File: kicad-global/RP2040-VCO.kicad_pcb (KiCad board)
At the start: 2 copper layers, 207 x 128.5 mm, 46 parts, among them J1 V/oct, J2 Power Input, J3 Inv CV, J4 Out, U1 TL074, U2 Seed_XIAO_RP2040

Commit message: finished schem and started pcb
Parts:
- added C11: 100pF, Capacitor_SMD:C_0805_2012Metric_Pad1.18x1.45mm_HandSolder, F.Cu at (55.0, 170.0)
- added CHORD1: 10k, Kicad-perso:Pot-bourns-alpha, F.Cu at (42.5, 70.5)
- added INV1: 10k, Kicad-perso:Pot-bourns-alpha, F.Cu at (42.5, 88.3)
- added SW1: SW_SPDT, Kicad-perso:SW_Toggle_Blue_wSlots, F.Cu at (40.6, 109.2)
- added SW2: SW_MEC_LOW_PROF_LED, Kicad-perso:PB01-109TL, F.Cu at (45.7, 121.9)
- added U3: AP2210K-5.0TRG1, Kicad-perso:SOT95P282X130-5N, F.Cu at (50.0, 170.0)
- C3, C4: footprint Capacitor_THT:CP_Radial_D5.0mm_P2.00mm -> Capacitor_SMD:CP_Elec_4x5.4
- C8: renamed from C11; value 10uF -> 1uF
- J1, J3, J4: footprint Synth:Thonkiconn -> Kicad-perso:Thonkiconn
- TUNE1: footprint Synth:Pot-bourns-alpha -> Kicad-perso:Pot-bourns-alpha
- moved J4 108.3 mm to (35.6, 116.8)
- moved J1 106.3 mm to (35.6, 131.4)
- moved TUNE1 99.3 mm to (43.1, 51.8)
- moved J3 90.0 mm to (45.7, 131.4)
- moved R8 39.1 mm to (80.0, 115.0), turned to -90 degrees
- moved C3 38.9 mm to (71.1, 91.4)
- moved J2 17.0 mm to (34.3, 98.3), turned to -90 degrees
- moved U1 13.6 mm to (70.0, 175.0)
- moved C4 9.37 mm to (71.7, 100.3)
- renumbered C8 to C12, C12 to C13, C13 to C14, C14 to C15, C15 to C16, R15 to R12, R12 to R13, R13 to R14, R14 to R15
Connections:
- C12 pad 1: +12V -> +5V
- C8 pad 1: +5V -> +12V
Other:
- outline, holes or cut-outs redrawn
- board text added: "4HP"
- board text removed: "12HP"
- board text removed: "board 2/2"

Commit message: update schem + begin routing
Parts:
- removed H2, H3: MountingHole_Pad, Synth:Doepfer Mounting hole
- added J4: Conn_01x06_Female, Connector_PinSocket_2.54mm:PinSocket_1x06_P2.54mm_Vertical, B.Cu at (75.8, 49.5)
- added J5: Conn_01x08_Female, Connector_PinSocket_2.54mm:PinSocket_1x08_P2.54mm_Vertical, B.Cu at (75.8, 95.6)
- added J6: Conn_01x06_Male, Connector_PinHeader_2.54mm:PinHeader_1x06_P2.54mm_Horizontal, B.Cu at (36.1, 49.5)
- added J7: Conn_01x08_Male, Connector_PinHeader_2.54mm:PinHeader_1x08_P2.54mm_Horizontal, B.Cu at (36.1, 95.6)
- C3, C4, J2, U2: moved to F.Cu
- moved R13 133.4 mm to (58.5, 51.8)
- moved R1 133.0 mm to (40.0, 54.6)
- moved C7 129.7 mm to (58.5, 55.9), turned to 180 degrees
- moved R5 127.6 mm to (40.0, 52.1)
- moved R16 126.8 mm to (47.1, 51.9)
- moved D4 121.0 mm to (58.1, 64.4)
- moved R2 120.7 mm to (40.0, 57.1)
- moved U1 120.3 mm to (52.8, 55.9)
- moved R6 120.3 mm to (51.0, 61.6)
- moved R11 119.3 mm to (58.5, 53.8)
- moved D3 118.7 mm to (58.1, 66.8)
- moved R8 118.3 mm to (58.5, 60.0)
- moved R15 118.1 mm to (47.1, 53.9)
- moved R14 116.0 mm to (58.5, 62.0), turned to 180 degrees
- moved R7 112.7 mm to (58.5, 58.0)
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- renumbered C9 to C8, C8 to C9, J4 to J8, R8 to R10, R10 to R12, R15 to R14, R14 to R15, R9 to R8, R12 to R9
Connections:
- net Net-(C16-Pad1) renamed /OutJack
- net Net-(CHORD1-Pad2) renamed /ChordPot
- net Net-(INV1-Pad2) renamed /InvPot
- net Net-(J1-PadT) renamed /V/octJack
- net Net-(J3-PadT) renamed /InvJack
- net Net-(R1-Pad1) renamed /TunePot
- C15 pad 2: Net-(C15-Pad2) -> GND
- D4 pad 2: Net-(C15-Pad2) -> GND
- R14 pad 1: Net-(C15-Pad2) -> GND
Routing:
- net +12V: track 0.00 -> 24.2 mm
- net -12V: track 0.00 -> 9.18 mm
- net Net-(R11-Pad2): track 0.00 -> 5.17 mm
- net /InvPot: track 0.00 -> 2.92 mm
- net /TunePot: track 0.00 -> 2.91 mm
- net /ChordPot: track 0.00 -> 2.91 mm
- net Net-(R11-Pad1): track 0.00 -> 2.41 mm
- net GND: vias 17 -> 9
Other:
- board size 207 x 128.5 mm -> 96.9 x 128.5 mm
- board text added: "RP2040 VCO V1.0 BleepSound 2023"
- board text added: "board 2/2"
- board text removed: "Double MS-20 VCF V1.2 BleepSound 2022"

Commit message: Routing finished
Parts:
- moved C16 38.0 mm to (39.6, 67.8)
- moved D2 28.5 mm to (44.0, 68.1)
- moved D1 28.5 mm to (44.0, 65.7)
- moved J7 27.8 mm to (36.3, 67.8)
- moved J5 27.8 mm to (75.8, 67.8)
- moved R3 26.6 mm to (39.6, 74.1)
- moved R4 26.6 mm to (39.6, 72.1)
- moved C3 21.7 mm to (40.9, 93.5), turned to 90 degrees
- moved C12 16.8 mm to (46.1, 91.1), turned to -90 degrees
- moved U3 13.6 mm to (49.0, 91.3), turned to 90 degrees
- moved C11 11.6 mm to (51.9, 91.1), turned to -90 degrees
- moved C9 10.8 mm to (48.9, 94.5), turned to 0 degrees
- moved C4 7.31 mm to (57.0, 93.5), turned to -90 degrees
- moved J2 3.81 mm to (54.0, 100.7), turned to -90 degrees
- moved J6 0.25 mm to (36.3, 49.5)
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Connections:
- J5 pad 1: +12V -> /OutJack
- J5 pad 2: GND -> /InvJack
- J5 pad 4: /InvJack -> GND
- J5 pad 5: /OutJack -> /SW_0
- J5 pad 7: /SW_0 -> /SW_1
- J5 pad 8: /SW_1 -> +12V
- J7 pad 1: +12V -> /OutJack
- J7 pad 2: GND -> /InvJack
- J7 pad 4: /InvJack -> GND
- J7 pad 5: /OutJack -> /SW_0
- J7 pad 7: /SW_0 -> /SW_1
- J7 pad 8: /SW_1 -> +12V
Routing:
- net +12V: track 24.2 -> 158.2 mm, vias 0 -> 2
- net /InvJack: track 0.00 -> 117.2 mm, vias 0 -> 2
- net +5V: track 0.00 -> 97.0 mm, vias 0 -> 1
- net +3V3: track 0.00 -> 84.7 mm, vias 0 -> 2
- net /V/octJack: track 0.00 -> 77.3 mm
- net /Push_SW: track 0.00 -> 77.0 mm
- net /OutJack: track 0.00 -> 71.3 mm
- net -12V: track 9.18 -> 66.8 mm, vias 0 -> 1
- net /SW_0: track 0.00 -> 55.4 mm
- net /InvPot: track 2.92 -> 48.1 mm
- net /V/oct: track 0.00 -> 44.7 mm
- net /SW_1: track 0.00 -> 41.3 mm
- net Net-(C14-Pad1): track 0.00 -> 38.9 mm, vias 0 -> 2
- net /Inv: track 0.00 -> 33.3 mm
- net /Tune: track 0.00 -> 31.9 mm
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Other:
- board size 96.9 x 128.5 mm -> 96.8 x 128.5 mm

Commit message: update VCO pcb
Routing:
- net GND: vias 69 -> 70

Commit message: update to v1.1
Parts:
- removed the J6 at (36.3, 49.5)
- removed the J7 at (36.3, 67.8)
- added H2: SpacerHoles, MountingHole:MountingHole_3.2mm_M3, F.Cu at (68.0, 96.0)
- added H3: SpacerHoles, MountingHole:MountingHole_3.2mm_M3, F.Cu at (90.5, 96.0)
- added J1: Conn_01x06_Male, Connector_PinHeader_2.54mm:PinHeader_1x06_P2.54mm_Vertical, F.Cu at (69.7, 49.5)
- added J2: Conn_01x08_Male, Connector_PinHeader_2.54mm:PinHeader_1x08_P2.54mm_Vertical, F.Cu at (53.3, 67.8)
- D1: renamed from D3; footprint Diode_SMD:D_SOD-123 -> Kicad-perso:D_SOD-123
- D2: renamed from D4; footprint Diode_SMD:D_SOD-123 -> Kicad-perso:D_SOD-123
- D3: renamed from D1; footprint Diode_SMD:D_SOD-123 -> Kicad-perso:D_SOD-123
- D4: renamed from D2; footprint Diode_SMD:D_SOD-123 -> Kicad-perso:D_SOD-123
- J8: renamed from J2; moved to B.Cu
- U1: footprint Package_SO:SOIC-14_3.9x8.7mm_P1.27mm -> Kicad-perso:SOIC-14_3.9x8.7mm_P1.27mm
- U3: renamed from U2; moved to B.Cu
- moved C10 43.4 mm to (56.9, 118.1), turned to 0 degrees
- moved C9 40.8 mm to (56.9, 115.6), turned to 0 degrees
- moved J8 40.6 mm to (60.3, 140.9), turned to 0 degrees
- moved C7 38.2 mm to (56.9, 113.0), turned to 0 degrees
- moved C14 36.2 mm to (54.0, 127.3)
- moved C13 36.0 mm to (64.4, 124.8)
- moved C12 36.0 mm to (58.6, 124.8)
- moved C16 36.0 mm to (61.4, 128.2)
- moved U2 36.0 mm to (61.5, 125.0)
- moved C6 36.0 mm to (57.0, 110.5), turned to 0 degrees
- moved C15 35.7 mm to (69.0, 127.2)
- moved C11 35.4 mm to (66.1, 118.1), turned to 180 degrees
- moved U3 32.7 mm to (61.5, 110.5), turned to 0 degrees
- moved C8 31.7 mm to (66.1, 113.0), turned to 180 degrees
- moved C5 29.3 mm to (66.1, 107.5), turned to 0 degrees
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- renumbered C16 to C1, C5 to C10, C8 to C11, C11 to C13, C3 to C14, C4 to C15, C9 to C16, C7 to C2, C6 to C3, C14 to C4, C13 to C5, C2 to C6, C15 to C7, C10 to C8, C1 to C9, J8 to J3, J1 to J4, J3 to J5, J4 to J6, J5 to J7, R5 to R1, R4 to R10, R6 to R11, R14 to R12, R3 to R13, R12 to R14, R10 to R15, R9 to R16, R1 to R2, R2 to R3, R13 to R4, R16 to R5, R11 to R6, R15 to R7, R7 to R8, R8 to R9, U3 to U2
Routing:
- net +3V3: track 84.7 -> 128.6 mm, vias 2 -> 0
- net /Chord: track 21.6 -> 61.2 mm, vias 0 -> 1
- net /Tune: track 31.9 -> 68.4 mm, vias 0 -> 1
- net /SW_1: track 41.3 -> 76.7 mm, vias 0 -> 2
- net /Inv: track 33.3 -> 66.9 mm, vias 0 -> 3
- net +12V: track 158.2 -> 133.8 mm, vias 2 -> 3
- net Net-(C1-Pad2): track 23.2 -> 2.90 mm
- net -12V: track 66.8 -> 84.6 mm, vias 1 -> 2
- net +5V: track 97.0 -> 111.7 mm, vias 1 -> 0
- net /SW_0: track 55.4 -> 67.8 mm
- net /Push_SW: track 77.0 -> 87.9 mm
- net GND: track 3.90 -> 14.7 mm, vias 70 -> 55
- net Net-(U1B-+): track 11.9 -> 22.2 mm
- net /InvJack: track 117.2 -> 107.3 mm, vias 2 -> 0
- net /V/oct: track 44.7 -> 49.8 mm
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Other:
- board size 96.8 x 128.5 mm -> 80 x 128.5 mm
- board text added: "RP2040 VCO V1.1 BleepSound 2023"

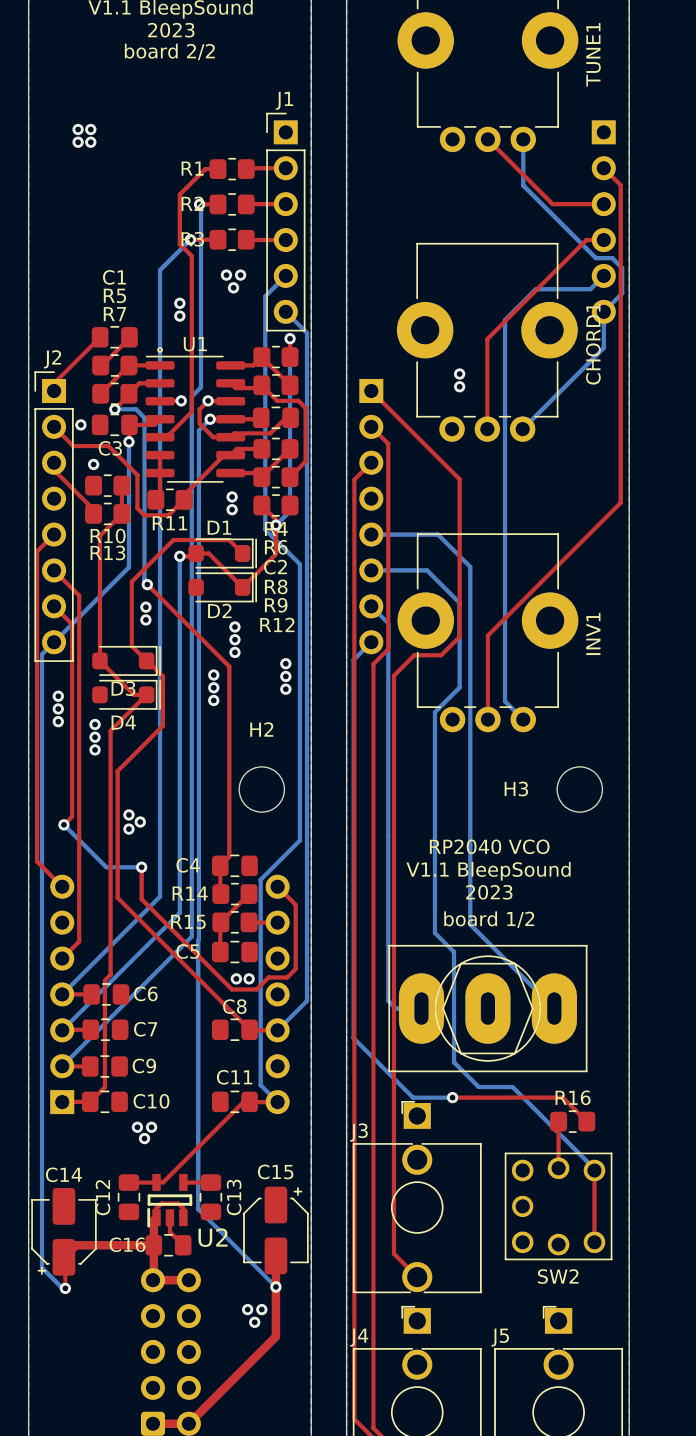
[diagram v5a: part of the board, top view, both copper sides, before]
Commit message: update board with pullup on switch
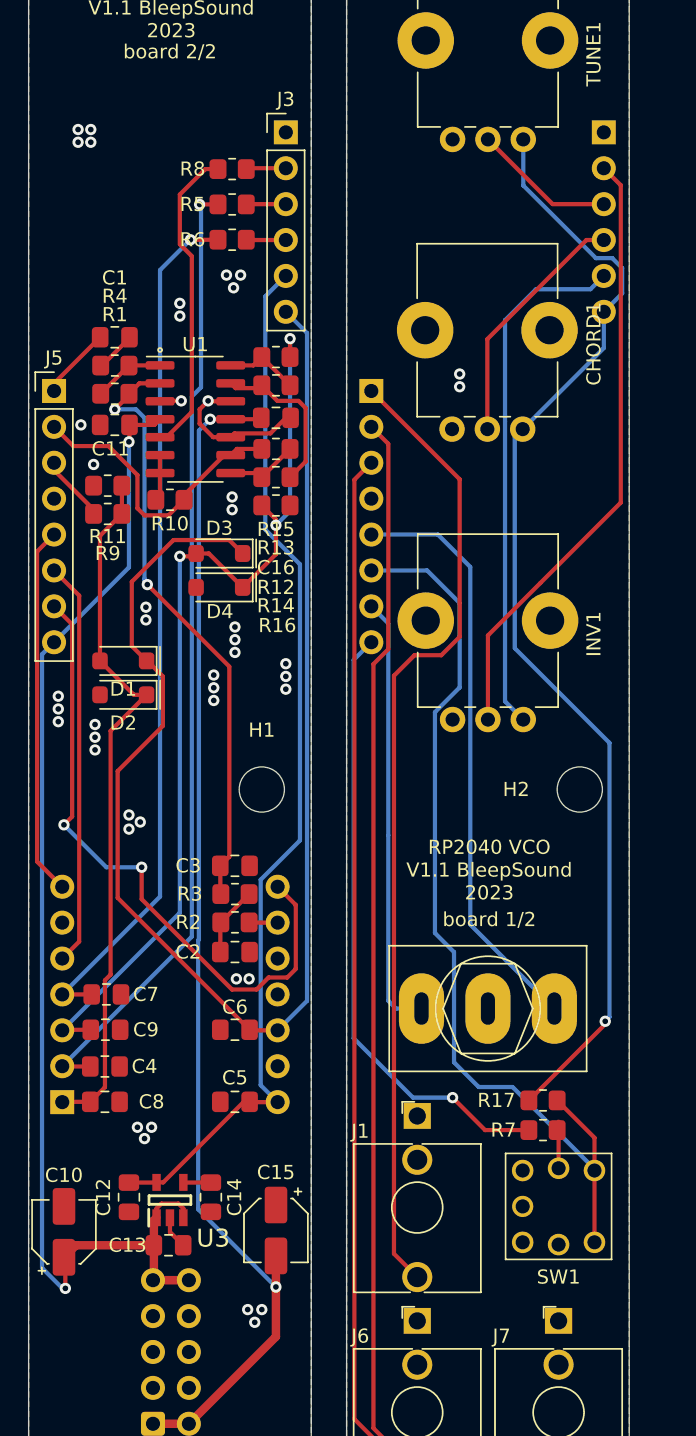
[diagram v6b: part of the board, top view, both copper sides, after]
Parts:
- added R17: 10k, Resistor_SMD:R_0805_2012Metric_Pad1.20x1.40mm_HandSolder, F.Cu at (87.9, 118.0)
- moved R7 2.18 mm to (87.9, 120.1), turned to 180 degrees
- renumbered C14 to C10, C3 to C11, C16 to C13, C13 to C14, C2 to C16, C5 to C2, C4 to C3, C9 to C4, C11 to C5, C8 to C6, C6 to C7, C10 to C8, C7 to C9, D3 to D1, D4 to D2, D1 to D3, D2 to D4, H2 to H1, H3 to H2, H1 to H3, J3 to J1, J6 to J2, J1 to J3, J7 to J4, J2 to J5, J4 to J6, J5 to J7, R7 to R1, R11 to R10, R10 to R11, R8 to R12, R6 to R13, R9 to R14, R4 to R15, R12 to R16, R15 to R2, R14 to R3, R5 to R4, R2 to R5, R3 to R6, R16 to R7, R1 to R8, R13 to R9, SW2 to SW1, SW1 to SW2, U3 to U2, U2 to U3
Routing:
- net +3V3: track 128.6 -> 181.5 mm, vias 0 -> 1
- net /Push_SW: track 87.9 -> 94.0 mm
- net +12V: track 133.8 -> 129.9 mm

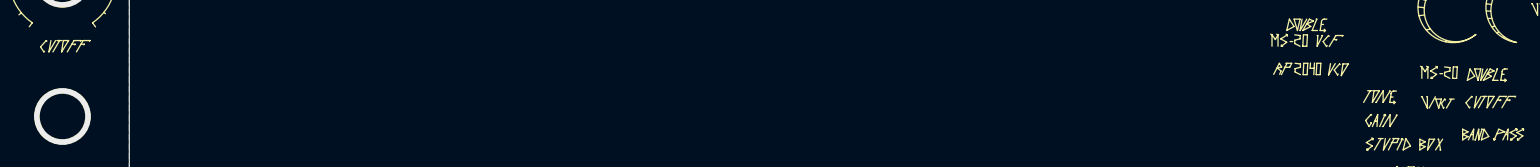
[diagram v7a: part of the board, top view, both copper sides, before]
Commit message: update label for tune (fix issue)
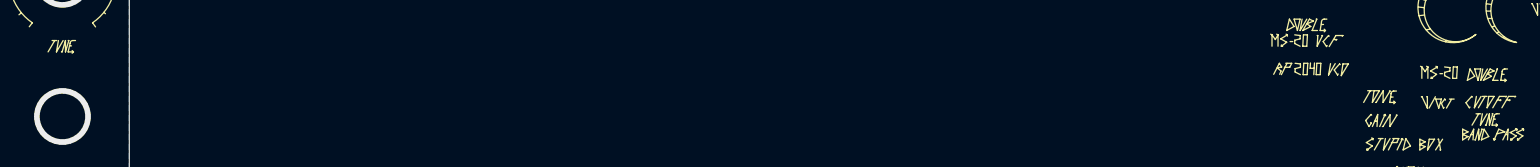
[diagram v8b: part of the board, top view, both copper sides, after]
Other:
- board text removed: "RP2040 VCO V1.0 BleepSound 2023"
